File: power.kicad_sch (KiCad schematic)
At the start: 25 parts, among them J2 USB_C_Receptacle_USB2.0, J4 Conn_01x02_Pin, Q5 FSS2301S, SW5 SW_SPST, U3 TP4056, U4 DW01A, U5 FS8205A, U6 LP2985-3.3

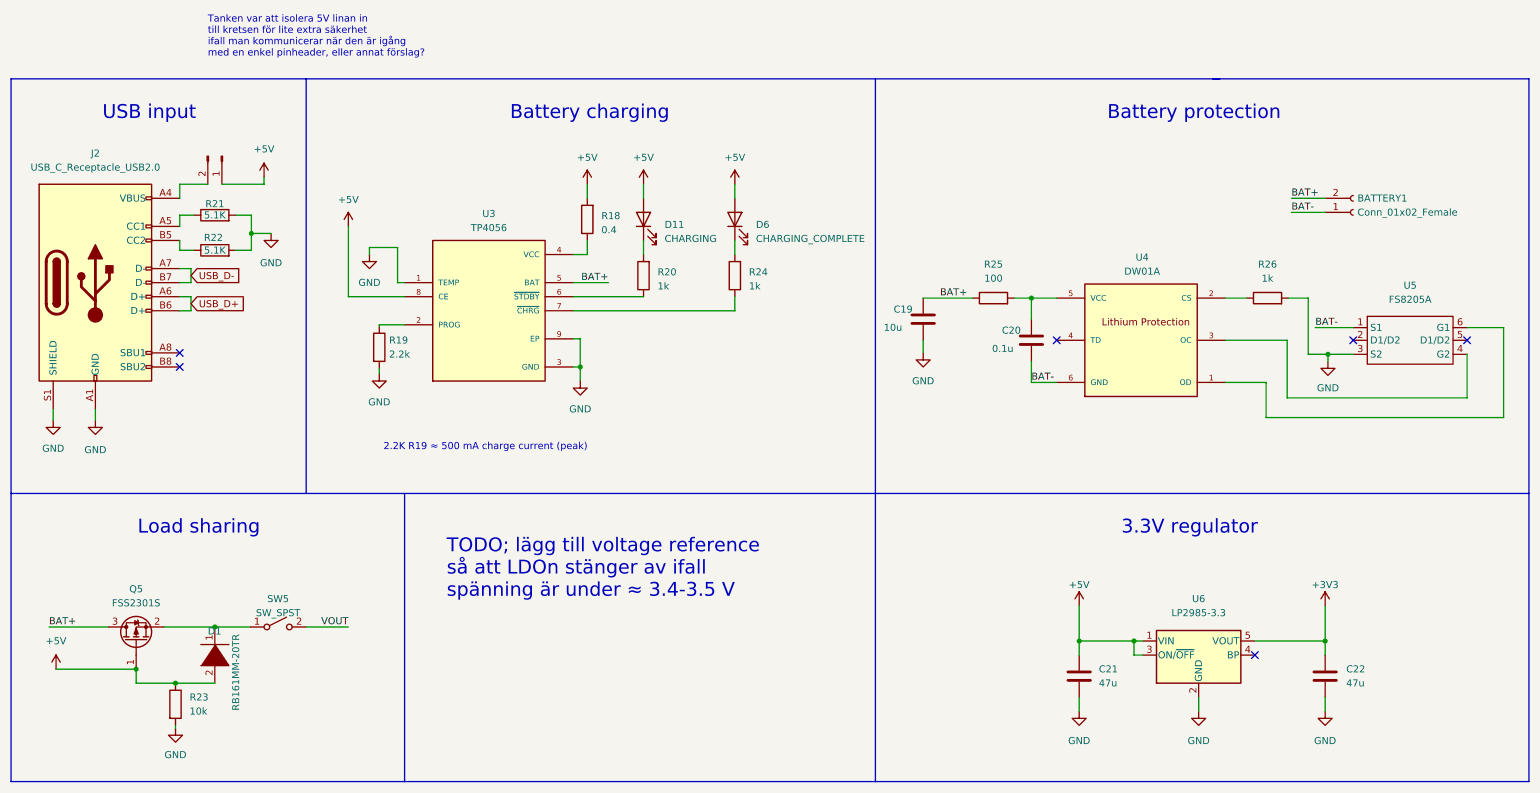
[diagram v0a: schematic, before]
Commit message: Swapped charging IC for reduced footprint
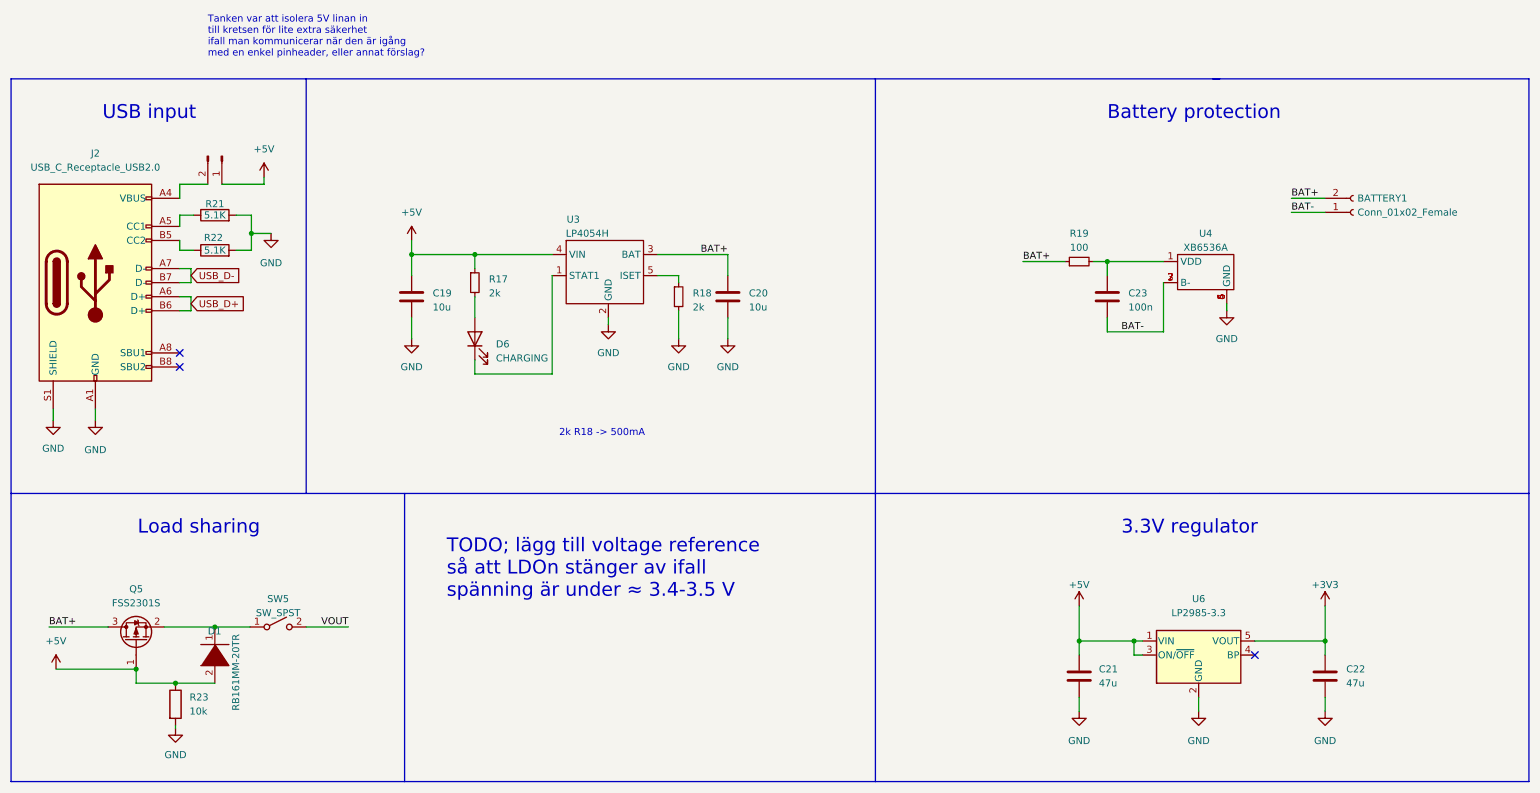
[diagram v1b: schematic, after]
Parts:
- removed D11: CHARGING, LED_SMD:LED_0603_1608Metric, symbol Device:LED
- removed R18: 0.4, Resistor_SMD:R_1206_3216Metric, symbol Device:R
- removed R19: 2.2k, Resistor_SMD:R_0603_1608Metric, symbol Device:R
- removed R20, R24, R26: 1k, Resistor_SMD:R_0603_1608Metric, symbol Device:R
- removed R25: 100, Resistor_SMD:R_0603_1608Metric, symbol Device:R
- removed U3: TP4056, LCSC:SOP127P600X175-9N, symbol TP4056:TP4056
- removed U4: DW01A, SOT23-6, symbol DW01:DW01A
- removed U5: FS8205A, Package_TO_SOT_SMD:SOT-23-6, symbol LCSC:FS8205A
- added C23: 100n, Capacitor_SMD:C_0603_1608Metric, symbol Device:C
- added R17, R18: 2k, Resistor_SMD:R_0603_1608Metric, symbol Device:R_Small
- added R19: 100, Resistor_SMD:R_0603_1608Metric, symbol Device:R_Small
- added U3: LP4054H, Package_TO_SOT_SMD:SOT-23-5, symbol LCSC:LP4054HB5F
- added U4: XB6536A, Package_DFN_QFN:DFN-6-1EP_2x2mm_P0.65mm_EP1x1.6mm, symbol LCSC:XB6536A
- C20: value 0.1u -> 10u
- D6: value CHARGING_COMPLETE -> CHARGING
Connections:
- net +5V: now also C19.1, R17.1, U3.4 (VIN); no longer D6.2 (A)
- net BAT+: now also C20.1, R19.1, U3.3 (BAT); no longer C19.1
- net BAT-: now also C23.2, U4.2 (B-), U4.3 (B-), U4.7 (B-); no longer C20.2
- net GND: now also C20.2, R18.2, U3.2 (GND), U4.4 (GND), U4.5 (GND), U4.6 (GND)
- net at D6.1 (K): now also U3.1 (STAT1)
- new net: C23.1, R19.2, U4.1 (VDD)
- new net: D6.2 (A), R17.2
- new net: R18.1, U3.5 (ISET)
- no-connect marks 6 -> 3
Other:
- note added: "2k R18 -> 500mA"
- note removed: "2.2K R19 ≈ 500 mA charge current (peak)"
- note removed: "Battery charging"

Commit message: finalized schematic + layout
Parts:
- added C15 (x2): 10u, Capacitor_SMD:C_0603_1608Metric, symbol Device:C
- added D11, D13: LESD9L5.0T5G, Diode_SMD:D_SOD-923, symbol Device:D
- added D14: PESDNC5D7VU, Diode_SMD:D_SOD-523, symbol Device:D
- added U5: ME2807, Package_TO_SOT_SMD:SOT-23-3, symbol LCSC:ME2807
- added U7: LPW5206, Package_TO_SOT_SMD:SOT-23-5, symbol LCSC:LPW5206
- D1: value RB161MM-20TR -> DS14W
- SW5: value SW_SPST -> SSSS811101; footprint (none) -> Button_Switch_SMD:SW_SPDT_PCM12
- U6: value LP2985-3.3 -> LP3992-3.3
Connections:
- net +5V: now also C15.1, U7.1 (VOUT); no longer C21.1, J4.1 (Pin_1), U6.1 (VIN), U6.3 (ON/~{OFF})
- net GND: now also C15.2, C15.2, D11.2 (A), D13.2 (A), D14.2 (A), U5.2 (GND), U7.2 (GND)
- net USB_D+: now also D13.1 (K)
- net USB_D-: now also D11.1 (K)
- net VOUT: now also C21.1, SW5.1 (B), U6.1 (VIN), U5.3 (VIN); no longer SW5.2 (B)
- net VBUS: now reaches J2.A4 (VBUS), J2.A9 (VBUS), J2.B4 (VBUS), J2.B9 (VBUS), J4.2 (Pin_2)
- net VBUS: now also D14.1 (K)
- net at D1.1 (A), Q5.2 (S): now also SW5.2 (A); no longer SW5.1 (A)
- new net: C15.1, J4.1 (Pin_1), U7.4 (EN), U7.5 (VIN)
- new net LDO_ENABLE: U5.1 (VOUT), U6.3 (ON/~{OFF})
- no-connect marks 3 -> 4
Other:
- note added: "Active fuse 600mA"
- note added: "Battery charging"
- note added: "TVS diodes"
- note added: "Voltage monitor for LDO"
- note removed: "TODO; lägg till voltage reference så att LDOn stänger av ifall spänning är under ≈ 3.4-3.5 V"
- note removed: "Tanken var att isolera 5V linan in till kretsen för lite extra säkerhet ifall man kommunicerar när den är igång med en enkel pinheader, eller annat förslag?"
- moved on the sheet: C19, C20, C21, C23, D6, R17, R18, R19, U3, U4

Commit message: Small tweaks
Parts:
- removed C15: 10u, Capacitor_SMD:C_0603_1608Metric, symbol Device:C
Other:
- moved on the sheet: R23
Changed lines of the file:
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@@
   (junction (at 43.942 48.26) (diameter 0) (color 0 0 0 0)
   )
-  (junction (at 113.03 31.75) (diameter 0) (color 0 0 0 0)
-  )
-  (junction (at 41.148 121.92) (diameter 0) (color 0 0 0 0)
+  (junction (at 40.64 121.92) (diameter 0) (color 0 0 0 0)
   )
   (junction (at 54.864 40.64) (diameter 0) (color 0 0 0 0)
@@
     (stroke (width 0) (type default))
   )
-  (wire (pts (xy 41.148 121.92) (xy 34.036 121.92))
+  (wire (pts (xy 34.036 121.92) (xy 40.64 121.92))
     (stroke (width 0) (type default))
   )
@@
     (stroke (width 0) (type default))
   )
-  (wire (pts (xy 113.03 44.45) (xy 113.03 40.64))
-    (stroke (width 0) (type default))
-  )
   (wire (pts (xy 248.92 107.95) (xy 248.92 114.3))
     (stroke (width 0) (type default))
@@
     (stroke (width 0) (type default))
   )
+  (wire (pts (xy 40.64 121.92) (xy 48.26 121.92))
+    (stroke (width 0) (type default))
+  )
   (wire (pts (xy 198.12 116.84) (xy 198.12 114.3))
     (stroke (width 0) (type default))
@@
     (stroke (width 0) (type default))
   )
-  (wire (pts (xy 41.148 129.54) (xy 41.148 130.048))
+  (wire (pts (xy 40.64 123.19) (xy 40.64 121.92))
+    (stroke (width 0) (type default))
+  )
+  (wire (pts (xy 40.64 130.81) (xy 40.64 131.318))
     (stroke (width 0) (type default))
   )
@@
     (stroke (width 0) (type default))
   )
-  (wire (pts (xy 48.26 121.92) (xy 41.148 121.92))
-    (stroke (width 0) (type default))
-  )
   (wire (pts (xy 52.07 31.75) (xy 72.39 31.75))
     (stroke (width 0) (type default))
@@
     (stroke (width 0) (type default))
   )
-  (wire (pts (xy 113.03 33.02) (xy 113.03 31.75))
-    (stroke (width 0) (type default))
-  )
   (polyline (pts (xy 77.47 86.36) (xy 229.87 86.36))
     (stroke (width 0) (type default))
@@
     (stroke (width 0) (type default))
   )
-  (wire (pts (xy 113.03 29.21) (xy 113.03 31.75))
-    (stroke (width 0) (type default))
-  )
-  (wire (pts (xy 113.03 31.75) (xy 102.87 31.75))
+  (wire (pts (xy 106.68 29.21) (xy 106.68 31.75))
     (stroke (width 0) (type default))
   )
@@
   )
   (wire (pts (xy 198.12 114.3) (xy 215.9 114.3))
+    (stroke (width 0) (type default))
+  )
+  (wire (pts (xy 106.68 31.75) (xy 102.87 31.75))
     (stroke (width 0) (type default))
   )
@@
     (effects (font (size 2.5 2.5)) (justify left bottom))
   )
-  (text "Active fuse 600mA" (at 86.36 20.32 0)
-    (effects (font (size 1.27 1.27)) (justify left bottom))
-  )
-  (text "TVS diodes\n" (at 109.22 69.85 0)
-    (effects (font (size 1.27 1.27)) (justify left bottom))
+  (text "Active fuse 600mA" (at 78.74 20.32 0)
+    (effects (font (size 2.5 2.5)) (justify left bottom))
+  )
+  (text "TVS diodes\n" (at 105.41 72.39 0)
+    (effects (font (size 2 2)) (justify left bottom))
   )
   (text "3.3V regulator\n" (at 212.09 95.25 0)
@@
     )
   )
-  (symbol (lib_id "Device:C") (at 113.03 36.83 0) (unit 1)
-    (in_bom yes) (on_board yes) (dnp no) (fields_autoplaced)
-    (property "Reference" "C15" (at 116.84 36.195 0)
-      (effects (font (size 1.27 1.27)) (justify left))
-    )
-    (property "Value" "10u" (at 116.84 38.735 0)
-      (effects (font (size 1.27 1.27)) (justify left))
-    )
-    (property "Footprint" "Capacitor_SMD:C_0603_1608Metric" (at 113.9952 40.64 0)
-      (effects (font (size 1.27 1.27)) hide)
-    )
-    (property "Datasheet" "~" (at 113.03 36.83 0)
-      (effects (font (size 1.27 1.27)) hide)
-    )
-    (pin "1")
-    (pin "2")
-    (instances
-      (project "picoemp_kicad"
-        (path "/3227ed55-0ca5-48b6-9dc2-dcbe4715d7c3/7a73d60b-1200-44ba-88e7-a313c65da933"
-          (reference "C15") (unit 1)
-        )
-        (path "/3227ed55-0ca5-48b6-9dc2-dcbe4715d7c3/5cadf0c8-edcd-4b51-b3d4-914d3d6ead13"
-          (reference "C25") (unit 1)
-        )
-      )
-      (project "Temperature probe rp2040"
-        (path "/460313fe-a917-4c7a-9f7f-e32c88e78d52"
-          (reference "C17") (unit 1)
-        )
-      )
-    )
-  )
   (symbol (lib_name "GND_2") (lib_id "power:GND") (at 93.98 44.45 0) (unit 1)
     (in_bom yes) (on_board yes) (dnp no) (fields_autoplaced)
@@
     )
   )
-  (symbol (lib_id "power:GND") (at 41.148 130.048 0) (unit 1)
-    (in_bom yes) (on_board yes) (dnp no) (fields_autoplaced)
-    (property "Reference" "#PWR057" (at 41.148 136.398 0)
-      (effects (font (size 1.27 1.27)) hide)
-    )
-    (property "Value" "GND" (at 41.148 134.874 0)
-      (effects (font (size 1.27 1.27)))
-    )
-    (property "Footprint" "" (at 41.148 130.048 0)
-      (effects (font (size 1.27 1.27)) hide)
-    )
-    (property "Datasheet" "" (at 41.148 130.048 0)
+  (symbol (lib_id "power:GND") (at 40.64 131.318 0) (unit 1)
+    (in_bom yes) (on_board yes) (dnp no) (fields_autoplaced)
+    (property "Reference" "#PWR057" (at 40.64 137.668 0)
+      (effects (font (size 1.27 1.27)) hide)
+    )
+    (property "Value" "GND" (at 40.64 136.144 0)
+      (effects (font (size 1.27 1.27)))
+    )
+    (property "Footprint" "" (at 40.64 131.318 0)
+      (effects (font (size 1.27 1.27)) hide)
+    )
+    (property "Datasheet" "" (at 40.64 131.318 0)
       (effects (font (size 1.27 1.27)) hide)
     )
@@
     )
   )
-  (symbol (lib_name "GND_2") (lib_id "power:GND") (at 113.03 44.45 0) (unit 1)
-    (in_bom yes) (on_board yes) (dnp no) (fields_autoplaced)
-    (property "Reference" "#PWR072" (at 113.03 50.8 0)
-      (effects (font (size 1.27 1.27)) hide)
-    )
-    (property "Value" "GND" (at 113.03 49.53 0)
-      (effects (font (size 1.27 1.27)))
-    )
-    (property "Footprint" "" (at 113.03 44.45 0)
-      (effects (font (size 1.27 1.27)) hide)
-    )
-    (property "Datasheet" "" (at 113.03 44.45 0)
-      (effects (font (size 1.27 1.27)) hide)
-    )
-    (pin "1")
-    (instances
-      (project "picoemp_kicad"
-        (path "/3227ed55-0ca5-48b6-9dc2-dcbe4715d7c3/5cadf0c8-edcd-4b51-b3d4-914d3d6ead13"
-          (reference "#PWR072") (unit 1)
-        )
-      )
-    )
-  )
-  (symbol (lib_id "power:+5V") (at 113.03 29.21 0) (unit 1)
-    (in_bom yes) (on_board yes) (dnp no) (fields_autoplaced)
-    (property "Reference" "#PWR051" (at 113.03 33.02 0)
-      (effects (font (size 1.27 1.27)) hide)
-    )
-    (property "Value" "+5V" (at 113.03 24.13 0)
-      (effects (font (size 1.27 1.27)))
-    )
-    (property "Footprint" "" (at 113.03 29.21 0)
-      (effects (font (size 1.27 1.27)) hide)
-    )
-    (property "Datasheet" "" (at 113.03 29.21 0)
+  (symbol (lib_id "power:+5V") (at 106.68 29.21 0) (unit 1)
+    (in_bom yes) (on_board yes) (dnp no) (fields_autoplaced)
+    (property "Reference" "#PWR051" (at 106.68 33.02 0)
+      (effects (font (size 1.27 1.27)) hide)
+    )
+    (property "Value" "+5V" (at 106.68 24.13 0)
+      (effects (font (size 1.27 1.27)))
+    )
+    (property "Footprint" "" (at 106.68 29.21 0)
+      (effects (font (size 1.27 1.27)) hide)
+    )
+    (property "Datasheet" "" (at 106.68 29.21 0)
       (effects (font (size 1.27 1.27)) hide)
     )
@@
     )
   )
-  (symbol (lib_id "Device:R") (at 41.148 125.73 0) (unit 1)
-    (in_bom yes) (on_board yes) (dnp no) (fields_autoplaced)
-    (property "Reference" "R23" (at 43.688 124.4599 0)
-      (effects (font (size 1.27 1.27)) (justify left))
-    )
-    (property "Value" "10k" (at 43.688 126.9999 0)
-      (effects (font (size 1.27 1.27)) (justify left))
-    )
-    (property "Footprint" "Resistor_SMD:R_0603_1608Metric" (at 39.37 125.73 90)
-      (effects (font (size 1.27 1.27)) hide)
-    )
-    (property "Datasheet" "~" (at 41.148 125.73 0)
-      (effects (font (size 1.27 1.27)) hide)
-    )
+  (symbol (lib_id "Device:R") (at 40.64 127 0) (unit 1)
+    (in_bom yes) (on_board yes) (dnp no) (fields_autoplaced)
+    (property "Reference" "R23" (at 43.18 125.7299 0)
+      (effects (font (size 1.27 1.27)) (justify left))
+    )
+    (property "Value" "10k" (at 43.18 128.2699 0)
+      (effects (font (size 1.27 1.27)) (justify left))
+    )
+    (property "Footprint" "Resistor_SMD:R_0603_1608Metric" (at 38.862 127 90)
+      (effects (font (size 1.27 1.27)) hide)
+    )
+    (property "Datasheet" "~" (at 40.64 127 0)
+      (effects (font (size 1.27 1.27)) hide)
+    )

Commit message: finishing touches
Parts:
- removed J4: Conn_01x02_Pin, Connector_PinHeader_2.54mm:PinHeader_1x02_P2.54mm_Vertical, symbol Connector:Conn_01x02_Pin
- added D15: 5V_PWR, LED_SMD:LED_0603_1608Metric, symbol Device:LED
- added JP1: ~, Jumper:SolderJumper-2_P1.3mm_Open_Pad1.0x1.5mm, symbol Jumper:SolderJumper_2_Open
- added Q7: FSS2302S, Package_TO_SOT_SMD:SOT-23, symbol LCSC:FSS2302S
- added R24: 1k, Resistor_SMD:R_0603_1608Metric, symbol Device:R_Small
- added R25: 100k, Resistor_SMD:R_0603_1608Metric, symbol Device:R_Small
- added SW6: SSSS811101, Button_Switch_SMD:SW_SPDT_PCM12, symbol Switch:SW_SPST
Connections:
- net +5V: now also R24.1
- net GND: now also D15.1 (K), R25.1
- net VBUS: now also JP1.2 (B), Q7.2 (S), SW6.1 (B)
- net at C15.1, U7.4 (EN), U7.5 (VIN): now also JP1.1 (A), Q7.3 (D)
- new net: Q7.1 (G), R25.2, SW6.2 (A)
- new net: D15.2 (A), R24.2
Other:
- company: (none) -> Kevin Pettersson
- title: (none) -> Power
- moved on the sheet: D11, D13, D14
